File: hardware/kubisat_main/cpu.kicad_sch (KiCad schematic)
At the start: 33 parts, among them J2 Micro_SD_Card_Det1, J4 DEBUG_SWD, J5 UART0, SW1 BOOTSEL, SW2 RESET, U1 RP2040, U6 W25Q16JVSS, Y1 12MHz

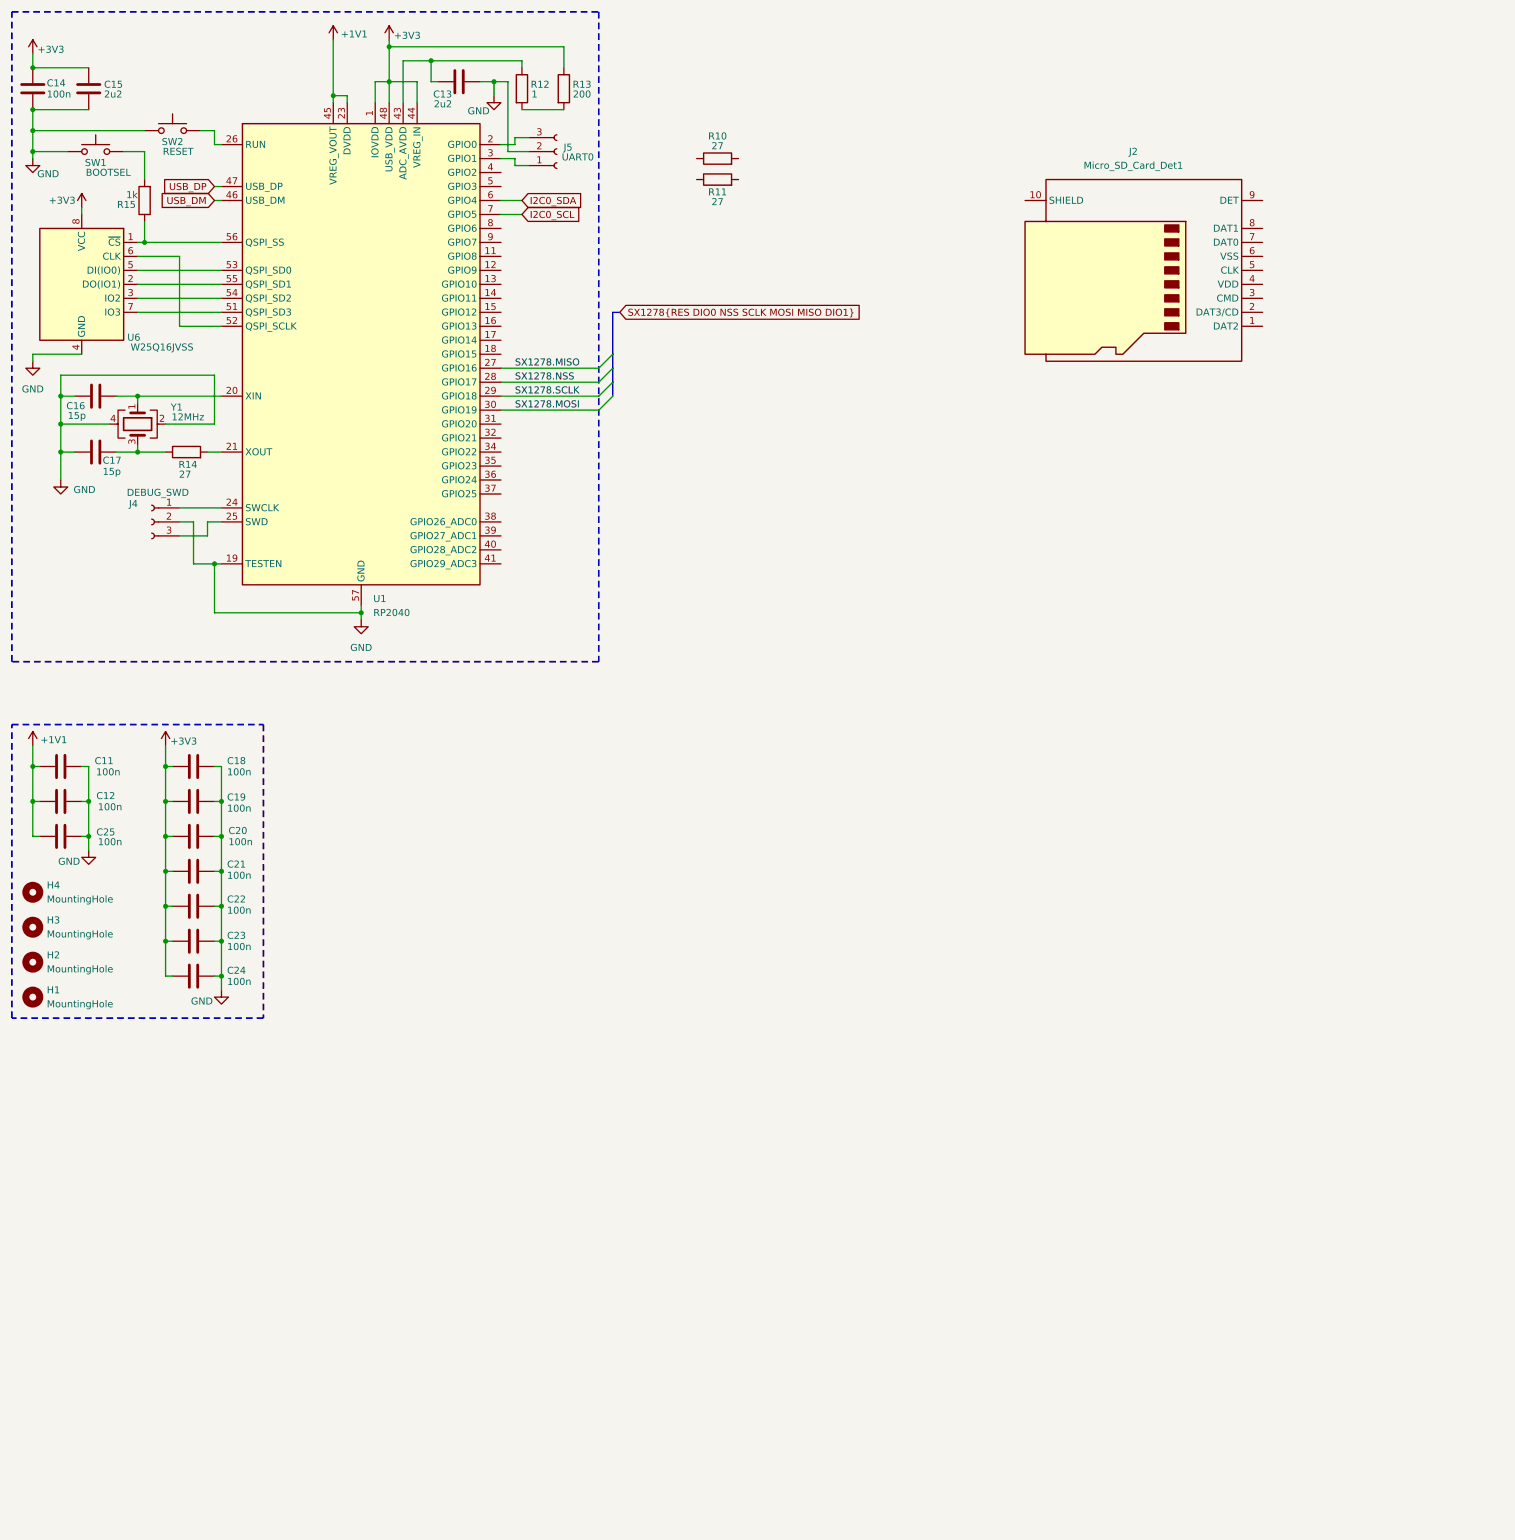
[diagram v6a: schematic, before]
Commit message: changed strucutre, split main into 2 sseparate boards
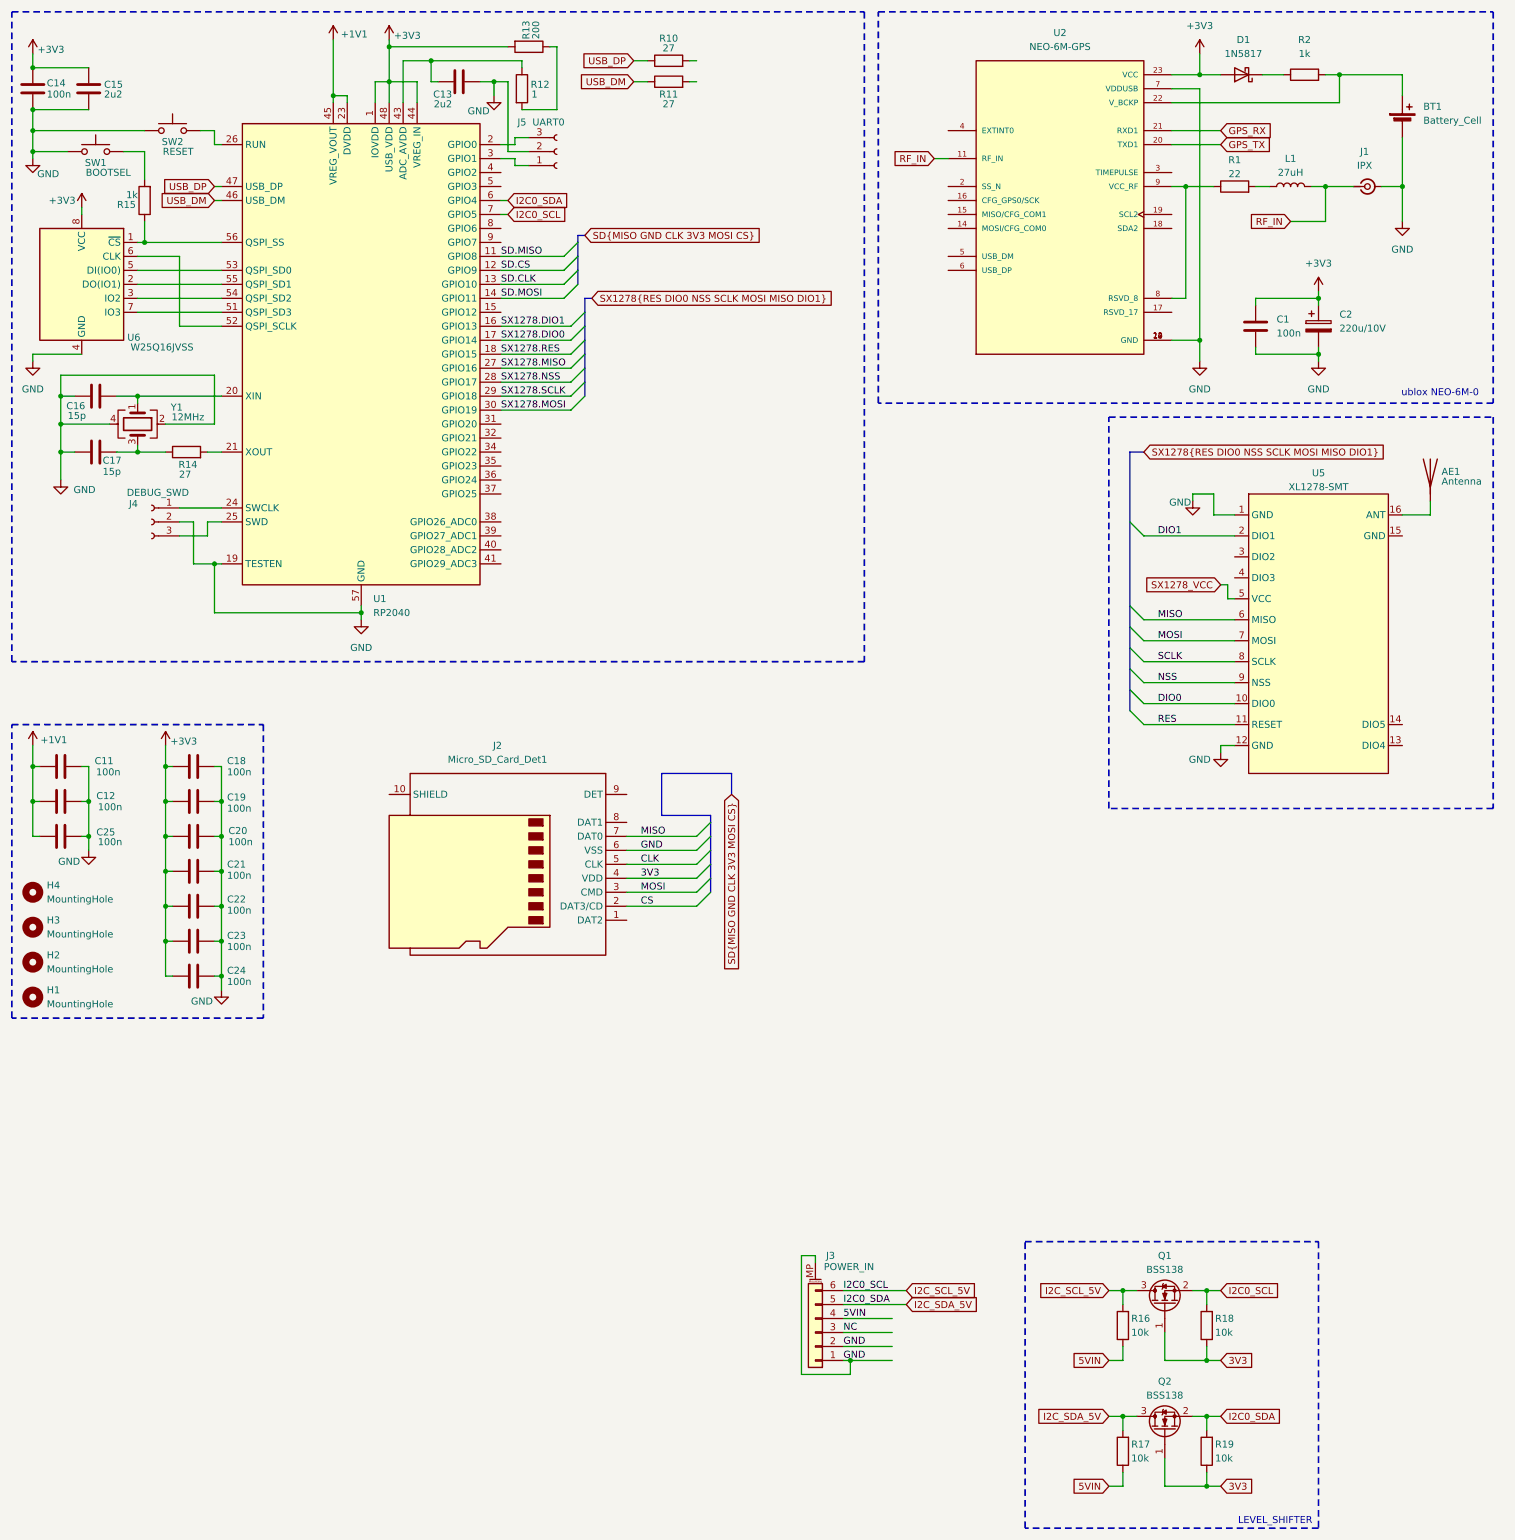
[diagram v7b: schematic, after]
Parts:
- added AE1: Antenna, symbol Device:Antenna
- added BT1: Battery_Cell, Battery:BatteryHolder_Seiko_MS621F, symbol Device:Battery_Cell
- added C1: 100n, Capacitor_SMD:C_0805_2012Metric, symbol Device:C
- added C2: 220u/10V, Capacitor_Tantalum_SMD:CP_EIA-6032-15_Kemet-U, symbol Device:C_Polarized
- added D1: 1N5817, Diode_SMD:D_SOD-123, symbol Device:D_Schottky
- added J1: IPX, Connector_Coaxial:U.FL_Hirose_U.FL-R-SMT-1_Vertical, symbol Connector:Conn_Coaxial_Small
- added J3: POWER_IN, Connector_JST:JST_PH_S6B-PH-SM4-TB_1x06-1MP_P2.00mm_Horizontal, symbol Connector_Generic_MountingPin:Conn_01x06_MountingPin
- added L1: 27uH, Inductor_SMD:L_0805_2012Metric, symbol Device:L
- added Q1, Q2: BSS138, Package_TO_SOT_SMD:SOT-23, symbol Transistor_FET:BSS138
- added R1: 22, Resistor_SMD:R_0805_2012Metric, symbol Device:R
- added R16, R17, R18, R19: 10k, symbol Device:R
- added R2: 1k, Resistor_SMD:R_0805_2012Metric, symbol Device:R
- added U2: NEO-6M-GPS, NEO-6M-GPS:XCVR_NEO-6M-GPS, symbol RF_GPS:NEO-6M-GPS
- added U5: XL1278-SMT, RF:XL1278-SMT, symbol RF:XL1278-SMT
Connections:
- net +3V3: now also R13.2, C1.1, C2.1, D1.2 (A), U2.23 (VCC); no longer R13.1
- net GND: now also J2.6 (VSS), BT1.2 (-), C1.2, C2.2, J1.2 (Ext), J3.1 (Pin_1), J3.2 (Pin_2), J3.MP (MountPin), U2.10 (GND), U2.12 (GND), U2.13 (GND), U2.24 (GND), U2.7 (VDDUSB), U5.1 (GND), U5.12 (GND)
- net I2C0_SCL: now also J3.6 (Pin_6), Q1.2 (S), Q1.3 (D), R16.2, R18.2
- net I2C0_SDA: now also J3.5 (Pin_5), Q2.2 (S), Q2.3 (D), R17.2, R19.2
- net USB_DM: now also R11.1
- net USB_DP: now also R10.1
- net at R12.2: now also R13.1; no longer R13.2
- net SD.MISO: now reaches U1.11 (GPIO8)
- net SD.CS: now reaches U1.12 (GPIO9)
- net SD.CLK: now reaches U1.13 (GPIO10)
- net SD.MOSI: now reaches U1.14 (GPIO11)
- net SX1278.DIO1: now reaches U1.16 (GPIO13)
- net SX1278.DIO0: now reaches U1.17 (GPIO14)
- net SX1278.RES: now reaches U1.18 (GPIO15)
- net CS: now reaches J2.2 (DAT3/CD)
- net MOSI: now reaches J2.3 (CMD)
- net MOSI: now also U5.7 (MOSI)
- net 3V3: now reaches J2.4 (VDD)
- net 3V3: now also Q1.1 (G), Q2.1 (G), R18.1, R19.1
- net CLK: now reaches J2.5 (CLK)
- net MISO: now reaches J2.7 (DAT0)
- net MISO: now also U5.6 (MISO)
- new net: R1.1, U2.8 (RSVD_8), U2.9 (VCC_RF)
- new net: L1.1, R1.2
- new net: AE1.1 (A), U5.16 (ANT)
- new net: D1.1 (K), R2.1
- new net: BT1.1 (+), R2.2, U2.22 (V_BCKP)
- new net 5VIN: J3.4 (Pin_4), R16.1, R17.1
- new net DIO0: U5.10 (DIO0)
- new net DIO1: U5.2 (DIO1)
- new net GPS_RX: U2.21 (RXD1)
- new net GPS_TX: U2.20 (TXD1)
- new net NC: J3.3 (Pin_3)
- new net NSS: U5.9 (NSS)
- new net RES: U5.11 (RESET)
- new net RF_IN: J1.1 (In), L1.2, U2.11 (RF_IN)
- new net SCLK: U5.8 (SCLK)
- new net SX1278_VCC: U5.5 (VCC)
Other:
- note added: "LEVEL_SHIFTER"
- note added: "ublox NEO-6M-0"
- moved on the sheet: J2, R10, R11, R13
